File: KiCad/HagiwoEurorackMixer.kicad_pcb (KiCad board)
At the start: 2 copper layers, 67.9 x 128.5 mm, 34 parts, among them J1 IN 1, J2 IN 2, J3 IN 3, J4 IN 4, J5 OUT, J6 EURO_PWR_2x5, U2 TL072

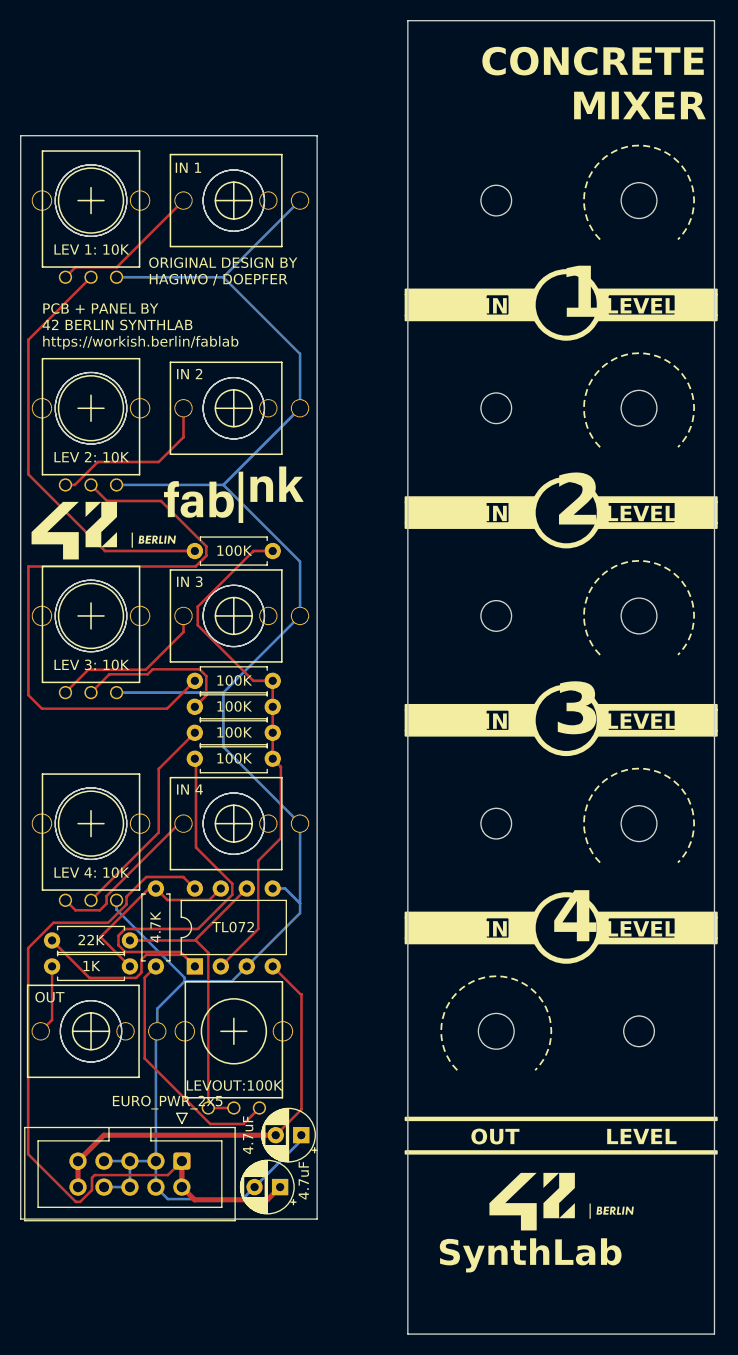
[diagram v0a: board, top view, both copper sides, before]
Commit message: Produced gerber files for test laser cutting - adapted all panel drill holes to 6mm
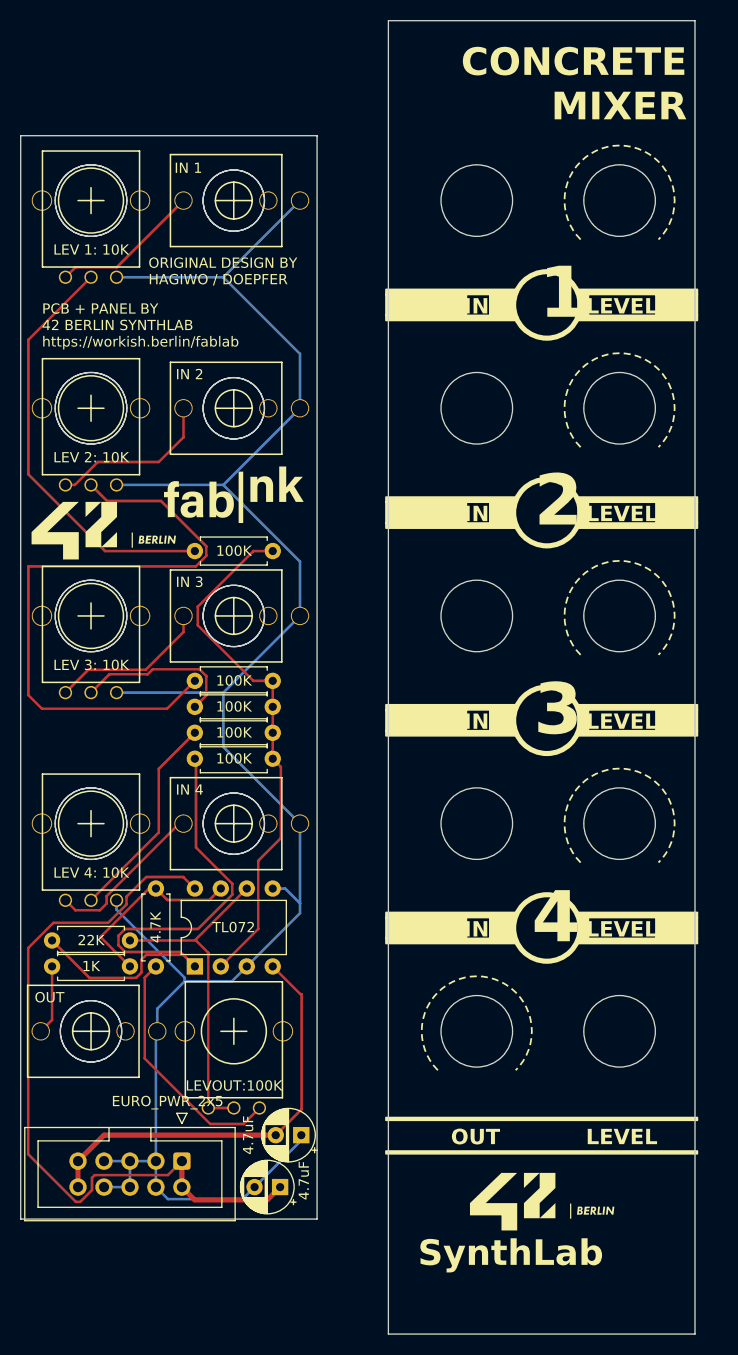
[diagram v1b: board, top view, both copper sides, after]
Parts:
- removed the REF** at (129.5, 114.1)
- removed the REF** at (115.6, 114.1)
- removed the REF** at (129.5, 53.2)
- removed the REF** at (129.5, 93.8)
- removed the REF** at (115.6, 134.4)
- removed the REF** at (115.6, 73.5)
- removed the REF** at (115.6, 53.2)
- removed the REF** at (129.5, 134.4)
- removed the REF** at (115.6, 93.8)
- removed the REF** at (129.5, 73.5)
- added REF**: MountingHole_6mm, Library:MountingHole_6mm, F.Cu at (113.7, 73.5)
- added REF**: MountingHole_6mm, Library:MountingHole_6mm, F.Cu at (113.7, 53.2)
- added REF**: MountingHole_6mm, Library:MountingHole_6mm, F.Cu at (127.6, 53.2)
- added REF**: MountingHole_6mm, Library:MountingHole_6mm, F.Cu at (113.7, 134.4)
- added REF**: MountingHole_6mm, Library:MountingHole_6mm, F.Cu at (127.6, 134.4)
- added REF**: MountingHole_6mm, Library:MountingHole_6mm, F.Cu at (127.6, 93.8)
- added REF**: MountingHole_6mm, Library:MountingHole_6mm, F.Cu at (127.6, 73.5)
- added REF**: MountingHole_6mm, Library:MountingHole_6mm, F.Cu at (113.7, 114.1)
- added REF**: MountingHole_6mm, Library:MountingHole_6mm, F.Cu at (127.6, 114.1)
- added REF**: MountingHole_6mm, Library:MountingHole_6mm, F.Cu at (113.7, 93.8)
- moved REF** 1.91 mm to (109.9, 38.6)
- moved REF** 1.91 mm to (130.2, 161.1)
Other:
- board size 67.9 x 128.5 mm -> 66 x 128.5 mm
